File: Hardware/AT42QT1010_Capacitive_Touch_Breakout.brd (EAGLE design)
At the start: 25.4 x 33 mm, 31 parts, among them Q1 600mA/40V, U1 AT42QT1010 - UDFN

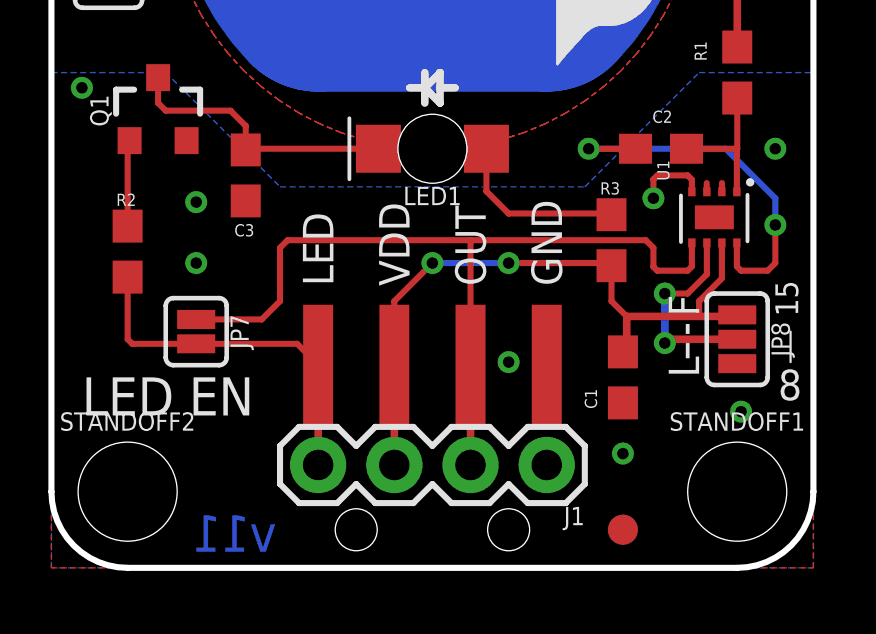
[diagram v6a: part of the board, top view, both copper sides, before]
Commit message: Fixing text, changing version number
...in preparation for review.
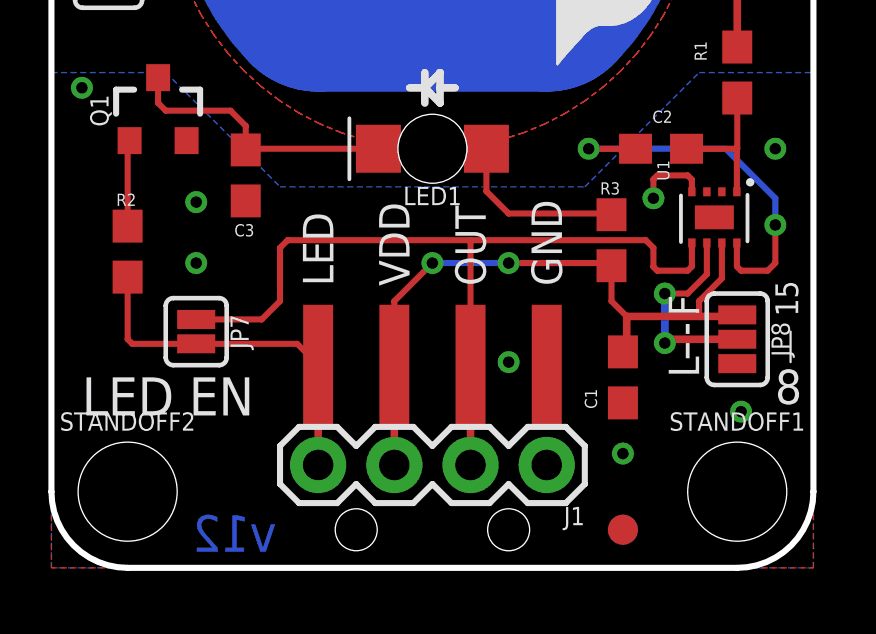
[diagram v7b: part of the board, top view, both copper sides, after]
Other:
- board text added: "v12"
- board text removed: "v11"
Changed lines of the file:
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@@
 <layer number="20" name="Dimension" color="15" fill="1" visible="yes" active="yes"/>
 <layer number="21" name="tPlace" color="16" fill="1" visible="yes" active="yes"/>
-<layer number="22" name="bPlace" color="14" fill="1" visible="yes" active="yes"/>
+<layer number="22" name="bPlace" color="14" fill="1" visible="no" active="yes"/>
 <layer number="23" name="tOrigins" color="15" fill="1" visible="yes" active="yes"/>
-<layer number="24" name="bOrigins" color="15" fill="1" visible="yes" active="yes"/>
-<layer number="25" name="tNames" color="7" fill="1" visible="no" active="yes"/>
+<layer number="24" name="bOrigins" color="15" fill="1" visible="no" active="yes"/>
+<layer number="25" name="tNames" color="7" fill="1" visible="yes" active="yes"/>
 <layer number="26" name="bNames" color="7" fill="1" visible="no" active="yes"/>
 <layer number="27" name="tValues" color="7" fill="1" visible="no" active="yes"/>
@@
 <layer number="43" name="vRestrict" color="2" fill="10" visible="no" active="yes"/>
 <layer number="44" name="Drills" color="7" fill="1" visible="no" active="yes"/>
-<layer number="45" name="Holes" color="7" fill="1" visible="yes" active="yes"/>
+<layer number="45" name="Holes" color="7" fill="1" visible="no" active="yes"/>
 <layer number="46" name="Milling" color="3" fill="1" visible="no" active="yes"/>
-<layer number="51" name="tDocu" color="6" fill="1" visible="yes" active="yes"/>
+<layer number="51" name="tDocu" color="6" fill="1" visible="no" active="yes"/>
 <layer number="52" name="bDocu" color="7" fill="1" visible="no" active="yes"/>
 <layer number="2" name="Route2" color="1" fill="3" visible="no" active="yes"/>
@@
 <text x="13.97" y="5.08" size="1.016" layer="22" font="vector" ratio="15" rot="MR270" align="center-right">OUT</text>
 <text x="16.51" y="5.08" size="1.016" layer="22" font="vector" ratio="15" rot="MR270" align="center-right">GND</text>
-<text x="6.096" y="1.143" size="1.2192" layer="16" font="vector" ratio="15" rot="MR0" align="center">v11</text>
+<text x="6.096" y="1.143" size="1.2192" layer="16" font="vector" ratio="15" rot="MR0" align="center">v12</text>
 <text x="22.86" y="24.638" size="1.016" layer="22" font="vector" ratio="15" rot="MR270" align="center-right">PAD</text>
 <text x="12.7" y="28.194" size="1.016" layer="21" font="vector" ratio="19" align="bottom-center">AT42QTXXXX
@@
 <text x="12.7" y="22.479" size="1.016" layer="21" font="vector" ratio="15">- 1011</text>
 <text x="24.892" y="8.382" size="0.762" layer="21" font="vector" ratio="15" rot="R90">15</text>
-<text x="25.019" y="6.604" size="1.016" layer="21" ratio="15" rot="R180">8</text>
+<text x="25.019" y="6.604" size="1.143" layer="21" ratio="15" rot="R180">8</text>
 <wire x1="24.638" y1="6.858" x2="24.638" y2="7.874" width="0.0762" layer="21"/>
 </plain>
@@
 <wire x1="18.63" y1="11.811" x2="18.669" y2="11.772" width="0.2032" layer="1"/>
 </signal>
-<signal name="N$1">
-<wire x1="21.844" y1="12.573" x2="21.844" y2="12.827" width="0.2032" layer="1"/>
-</signal>
-<signal name="N$2">
-<wire x1="22.352" y1="12.573" x2="22.352" y2="12.827" width="0.2032" layer="1"/>
-</signal>
 </signals>

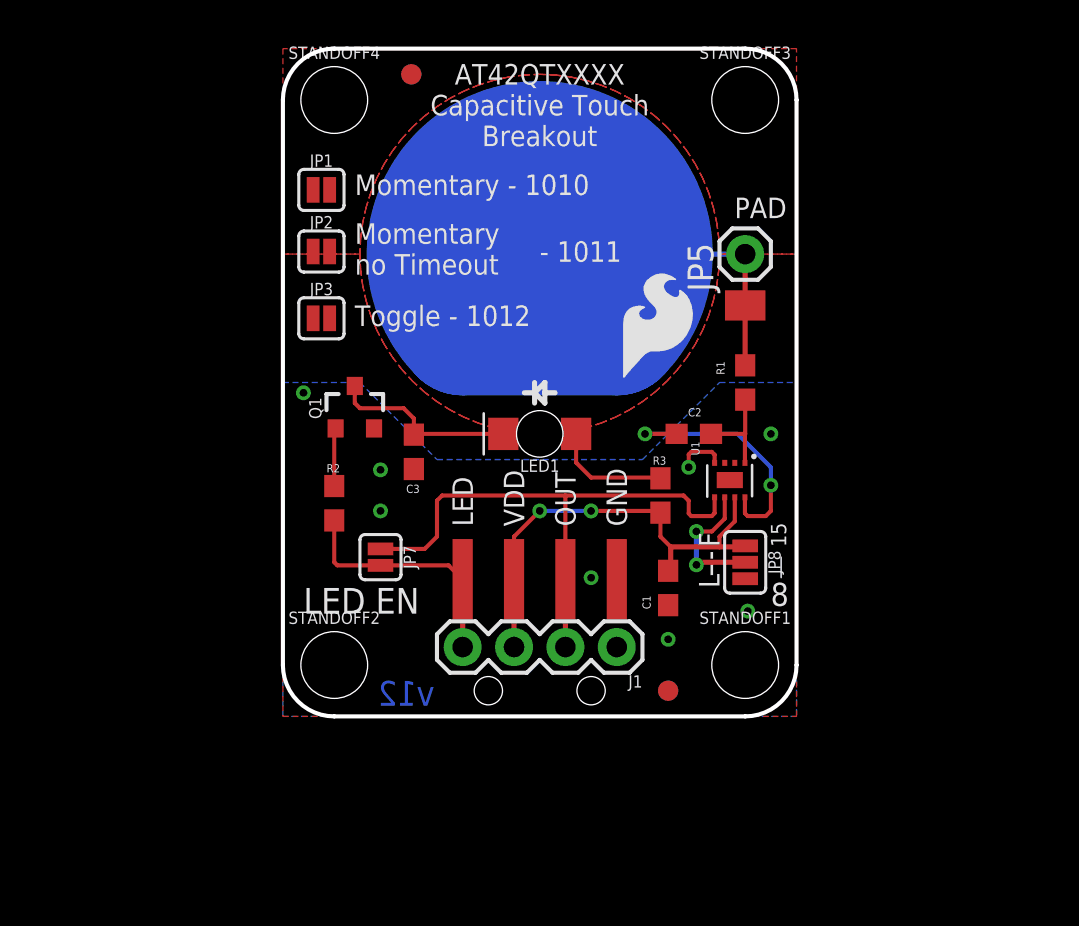
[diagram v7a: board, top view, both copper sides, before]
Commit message: Better Labels, replaced jumpers
Much better labels for the selection of low power/fast mode and 15min
timeout vs. no timeout. I also created a device that is a square solder
pad for production to use to identify different versions of the board.
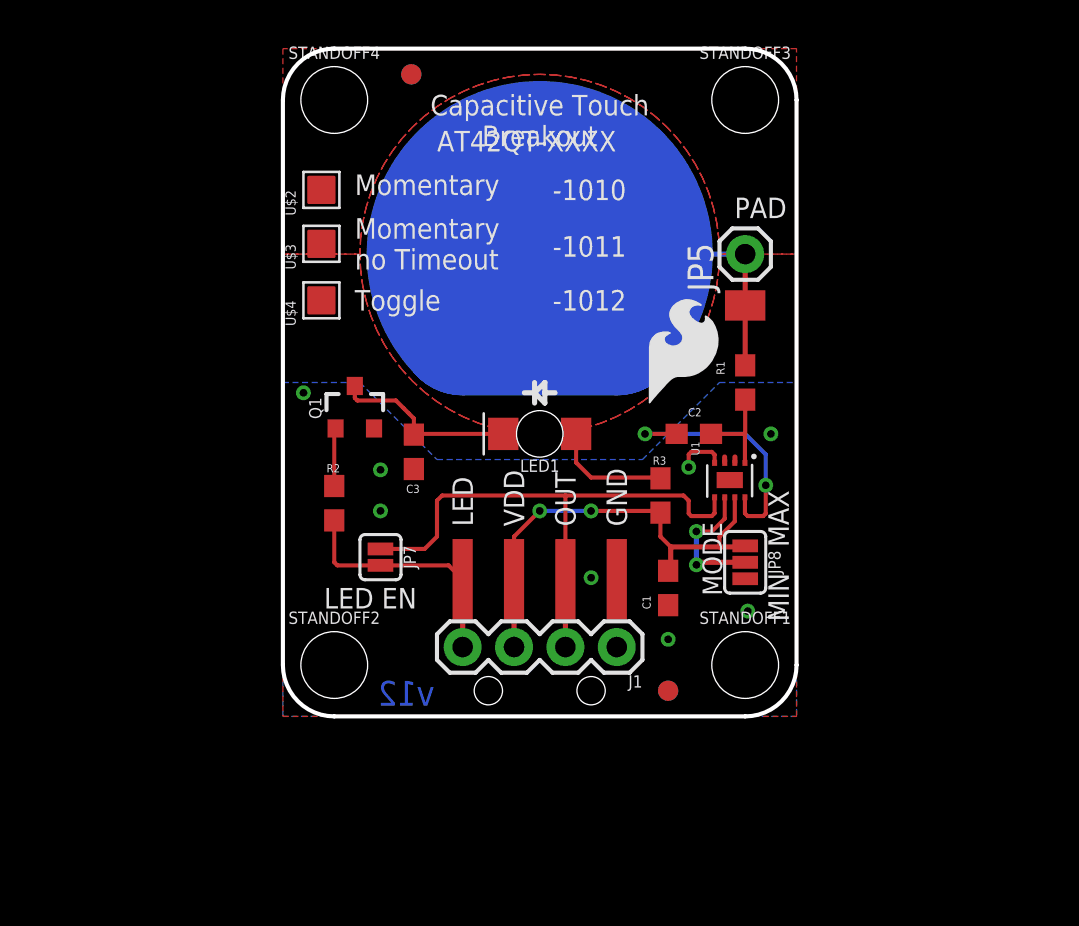
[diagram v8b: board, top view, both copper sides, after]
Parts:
- removed JP1, JP2, JP3: JUMPER-SMT_2_NO_SILK, SparkFun-Jumpers:SMT-JUMPER_2_NO_SILK
- added U$2, U$3, U$4: SOLDER_PAD_LABEL, local_parts:BLANK_SOLDER_PAD
- moved LOGO1 1.80 mm to (17.8, 15.2)
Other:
- board text added: "-1010"
- board text added: "-1011"
- board text added: "-1012"
- board text added: "AT42QT-XXXX"
- board text added: "Capacitive Touch Breakout"
- board text added: "MAX"
- board text added: "MIN"
- board text added: "MODE"
- board text added: "Momentary"
- board text added: "Toggle"
- board text removed: "- 1011"
- board text removed: "15"
- board text removed: "8"
- board text removed: "AT42QTXXXX Capacitive Touch Breakout"
- board text removed: "F"
- board text removed: "L"
- board text removed: "Momentary - 1010"
- board text removed: "Toggle - 1012"
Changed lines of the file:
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@@
 <layer number="20" name="Dimension" color="15" fill="1" visible="yes" active="yes"/>
 <layer number="21" name="tPlace" color="16" fill="1" visible="yes" active="yes"/>
-<layer number="22" name="bPlace" color="14" fill="1" visible="no" active="yes"/>
+<layer number="22" name="bPlace" color="14" fill="1" visible="yes" active="yes"/>
 <layer number="23" name="tOrigins" color="15" fill="1" visible="yes" active="yes"/>
-<layer number="24" name="bOrigins" color="15" fill="1" visible="no" active="yes"/>
-<layer number="25" name="tNames" color="7" fill="1" visible="yes" active="yes"/>
+<layer number="24" name="bOrigins" color="15" fill="1" visible="yes" active="yes"/>
+<layer number="25" name="tNames" color="7" fill="1" visible="no" active="yes"/>
 <layer number="26" name="bNames" color="7" fill="1" visible="no" active="yes"/>
 <layer number="27" name="tValues" color="7" fill="1" visible="no" active="yes"/>
@@
 <layer number="43" name="vRestrict" color="2" fill="10" visible="no" active="yes"/>
 <layer number="44" name="Drills" color="7" fill="1" visible="no" active="yes"/>
-<layer number="45" name="Holes" color="7" fill="1" visible="no" active="yes"/>
+<layer number="45" name="Holes" color="7" fill="1" visible="yes" active="yes"/>
 <layer number="46" name="Milling" color="3" fill="1" visible="no" active="yes"/>
-<layer number="51" name="tDocu" color="6" fill="1" visible="no" active="yes"/>
+<layer number="51" name="tDocu" color="6" fill="1" visible="yes" active="yes"/>
 <layer number="52" name="bDocu" color="7" fill="1" visible="no" active="yes"/>
 <layer number="2" name="Route2" color="1" fill="3" visible="no" active="yes"/>
@@
 <text x="6.096" y="1.143" size="1.2192" layer="16" font="vector" ratio="15" rot="MR0" align="center">v12</text>
 <text x="22.86" y="24.638" size="1.016" layer="22" font="vector" ratio="15" rot="MR270" align="center-right">PAD</text>
-<text x="12.7" y="28.194" size="1.016" layer="21" font="vector" ratio="19" align="bottom-center">AT42QTXXXX
-Capacitive Touch
-Breakout</text>
+<text x="12.7" y="28.194" size="1.016" layer="21" font="vector" ratio="19" align="bottom-center">Capacitive Touch
+Breakout
+</text>
 <text x="15.24" y="-17.78" size="1.778" layer="51" font="vector">Shawn Hymel</text>
 <rectangle x1="0" y1="0" x2="2.54" y2="2.54" layer="41"/>
@@
 <wire x1="12.446" y1="12.192" x2="11.938" y2="12.192" width="0.254" layer="51"/>
 <wire x1="12.954" y1="12.192" x2="13.462" y2="12.192" width="0.254" layer="51"/>
-<text x="21.59" y="8.382" size="1.016" layer="21" font="vector" ratio="15" rot="R90">F</text>
-<text x="21.59" y="6.35" size="1.016" layer="21" font="vector" ratio="15" rot="R90">L</text>
 <wire x1="0" y1="2.54" x2="0" y2="30.48" width="0.2032" layer="20"/>
 <wire x1="0" y1="30.48" x2="2.54" y2="33.02" width="0.2032" layer="20" curve="-90"/>
@@
 <dimension x1="2.54" y1="2.54" x2="2.54" y2="0" x3="-3.81" y3="1.27" textsize="1.27" textratio="15" layer="47" unit="inch"/>
 <dimension x1="2.54" y1="2.54" x2="0" y2="2.54" x3="1.27" y3="-6.35" textsize="1.27" textratio="15" layer="47" unit="inch"/>
-<wire x1="21.209" y1="6.985" x2="21.209" y2="8.128" width="0.127" layer="21" style="shortdash"/>
-<text x="1.016" y="5.08" size="1.27" layer="21" font="vector" ratio="15">LED EN</text>
+<text x="2.032" y="5.334" size="1.016" layer="21" font="vector" ratio="15">LED EN</text>
 <rectangle x1="19.431" y1="9.017" x2="19.812" y2="9.525" layer="41"/>
 <rectangle x1="22.098" y1="13.081" x2="22.479" y2="13.589" layer="41"/>
 <rectangle x1="21.971" y1="14.351" x2="22.352" y2="14.859" layer="41"/>
 <rectangle x1="7.62" y1="7.874" x2="8.001" y2="8.382" layer="41"/>
-<text x="3.556" y="25.781" size="1.016" layer="21" font="vector" ratio="15">Momentary - 1010</text>
-<text x="3.556" y="19.304" size="1.016" layer="21" font="vector" ratio="15">Toggle - 1012</text>
-<text x="3.556" y="21.844" size="1.016" layer="21" font="vector" ratio="15">Momentary
+<text x="3.556" y="25.781" size="1.016" layer="21" font="vector" ratio="15">Momentary</text>
+<text x="3.556" y="20.066" size="1.016" layer="21" font="vector" ratio="15">Toggle</text>
+<text x="3.556" y="22.098" size="1.016" layer="21" font="vector" ratio="15">Momentary
 no Timeout</text>
-<text x="12.7" y="22.479" size="1.016" layer="21" font="vector" ratio="15">- 1011</text>
-<text x="24.892" y="8.382" size="0.762" layer="21" font="vector" ratio="15" rot="R90">15</text>
-<text x="25.019" y="6.604" size="1.143" layer="21" ratio="15" rot="R180">8</text>
-<wire x1="24.638" y1="6.858" x2="24.638" y2="7.874" width="0.0762" layer="21"/>
+<text x="13.335" y="22.733" size="1.016" layer="21" font="vector" ratio="15">-1011</text>
+<text x="13.335" y="25.527" size="1.016" layer="21" font="vector" ratio="15">-1010</text>
+<text x="13.335" y="20.066" size="1.016" layer="21" font="vector" ratio="15">-1012</text>
+<text x="7.62" y="27.94" size="1.016" layer="21" font="vector" ratio="15">AT42QT-XXXX</text>
+<text x="21.717" y="5.969" size="0.9652" layer="21" font="vector" ratio="15" rot="R90">MODE</text>
+<text x="25.019" y="4.699" size="1.016" layer="21" font="vector" ratio="15" rot="R90">MIN</text>
+<text x="24.003" y="11.176" size="1.016" layer="21" font="vector" ratio="15" rot="R270">MAX</text>
 </plain>
 <attributes>
@@
 <attribute name="PROD_ID" value="CONN-09696" x="16.51" y="3.429" size="1.27" layer="27" ratio="15" rot="R180" display="off"/>
 </element>
-<element name="JP1" library="SparkFun-Jumpers" package="SMT-JUMPER_2_NO_SILK" value="JUMPER-SMT_2_NO_SILK" x="1.905" y="26.035"/>
-<element name="JP2" library="SparkFun-Jumpers" package="SMT-JUMPER_2_NO_SILK" value="JUMPER-SMT_2_NO_SILK" x="1.905" y="22.987"/>
-<element name="JP3" library="SparkFun-Jumpers" package="SMT-JUMPER_2_NO_SILK" value="JUMPER-SMT_2_NO_SILK" x="1.905" y="19.685"/>
 <element name="LOGO4" library="SparkFun-Aesthetics" package="SFE_LOGO_FLAME_.2" value="SFE_LOGO_FLAME.2_INCH" x="4.064" y="17.018" rot="MR0"/>
-<element name="LOGO1" library="SparkFun-Aesthetics" package="SFE_LOGO_FLAME_.2" value="SFE_LOGO_FLAME.2_INCH" x="16.51" y="16.51"/>
+<element name="LOGO1" library="SparkFun-Aesthetics" package="SFE_LOGO_FLAME_.2" value="SFE_LOGO_FLAME.2_INCH" x="17.78" y="15.24"/>
+<element name="U$2" library="local_parts" package="BLANK_SOLDER_PAD" value="SOLDER_PAD_LABEL" x="1.905" y="26.035" rot="R90"/>
+<element name="U$3" library="local_parts" package="BLANK_SOLDER_PAD" value="SOLDER_PAD_LABEL" x="1.905" y="23.368" rot="R90"/>
+<element name="U$4" library="local_parts" package="BLANK_SOLDER_PAD" value="SOLDER_PAD_LABEL" x="1.905" y="20.574" rot="R90"/>
 </elements>
 <signals>
@@
 <contactref element="C2" pad="2"/>
 <wire x1="19.47" y1="13.97" x2="19.558" y2="13.97" width="0.254" layer="1"/>
-<via x="24.13" y="11.43" extent="1-16" drill="0.381"/>
+<via x="23.876" y="11.43" extent="1-16" drill="0.381"/>
 <via x="17.907" y="13.97" extent="1-16" drill="0.381"/>
 <wire x1="17.907" y1="13.97" x2="19.47" y2="13.97" width="0.2032" layer="1"/>
-<wire x1="22.479" y1="13.97" x2="17.907" y2="13.97" width="0.2032" layer="16"/>
-<wire x1="22.987" y1="9.906" x2="23.876" y2="9.906" width="0.2032" layer="1"/>
-<wire x1="23.876" y1="9.906" x2="24.13" y2="10.16" width="0.2032" layer="1"/>
-<wire x1="24.13" y1="10.16" x2="24.13" y2="11.43" width="0.2032" layer="1"/>
-<wire x1="24.13" y1="11.43" x2="24.13" y2="12.319" width="0.2032" layer="16"/>
-<wire x1="24.13" y1="12.319" x2="22.479" y2="13.97" width="0.2032" layer="16"/>
+<wire x1="22.86" y1="13.97" x2="17.907" y2="13.97" width="0.2032" layer="16"/>
 <wire x1="22.848" y1="10.8324" x2="22.848" y2="10.045" width="0.2032" layer="1"/>
 <wire x1="22.848" y1="10.045" x2="22.987" y2="9.906" width="0.2032" layer="1"/>
+<wire x1="22.987" y1="9.906" x2="23.749" y2="9.906" width="0.2032" layer="1"/>
+<wire x1="23.749" y1="9.906" x2="23.876" y2="10.033" width="0.2032" layer="1"/>
+<wire x1="23.876" y1="10.033" x2="23.876" y2="11.43" width="0.2032" layer="1"/>
+<wire x1="23.876" y1="11.43" x2="23.876" y2="12.954" width="0.2032" layer="16"/>
+<wire x1="23.876" y1="12.954" x2="22.86" y2="13.97" width="0.2032" layer="16"/>
 </signal>
 <signal name="N$5">
@@
 <contactref element="C3" pad="1"/>
 <contactref element="LED1" pad="C"/>
-<wire x1="3.556" y1="16.34" x2="3.556" y2="15.494" width="0.2032" layer="1"/>
-<wire x1="3.556" y1="15.494" x2="3.81" y2="15.24" width="0.2032" layer="1"/>
 <wire x1="10.9" y1="13.97" x2="6.516" y2="13.97" width="0.2032" layer="1"/>
 <wire x1="6.516" y1="13.97" x2="6.477" y2="13.931" width="0.2032" layer="1"/>
-<wire x1="3.81" y1="15.24" x2="5.969" y2="15.24" width="0.2032" layer="1"/>
-<wire x1="5.969" y1="15.24" x2="6.477" y2="14.732" width="0.2032" layer="1"/>
+<wire x1="5.969" y1="15.24" x2="6.223" y2="14.986" width="0.2032" layer="1"/>
+<wire x1="6.223" y1="14.986" x2="6.477" y2="14.732" width="0.2032" layer="1"/>
 <wire x1="6.477" y1="14.732" x2="6.477" y2="13.931" width="0.2032" layer="1"/>
+<wire x1="3.556" y1="16.34" x2="3.556" y2="15.748" width="0.2032" layer="1"/>
+<wire x1="3.556" y1="15.748" x2="3.683" y2="15.621" width="0.2032" layer="1"/>
+<wire x1="3.683" y1="15.621" x2="5.588" y2="15.621" width="0.2032" layer="1"/>
+<wire x1="5.588" y1="15.621" x2="5.969" y2="15.24" width="0.2032" layer="1"/>
 </signal>
 <signal name="N$12">
@@
 <wire x1="18.63" y1="11.811" x2="18.669" y2="11.772" width="0.2032" layer="1"/>
 </signal>
+<signal name="N$1">
+<wire x1="21.844" y1="12.573" x2="21.844" y2="12.827" width="0.254" layer="1"/>
+</signal>
+<signal name="N$2">
+<wire x1="22.352" y1="12.573" x2="22.352" y2="12.827" width="0.254" layer="1"/>
+</signal>
 </signals>
